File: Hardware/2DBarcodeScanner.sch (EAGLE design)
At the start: 25 parts, among them J1 BARCODE_ENGINE_CONN, Q1 600mA/40V, Q2 600mA/40V, U1 3.3V

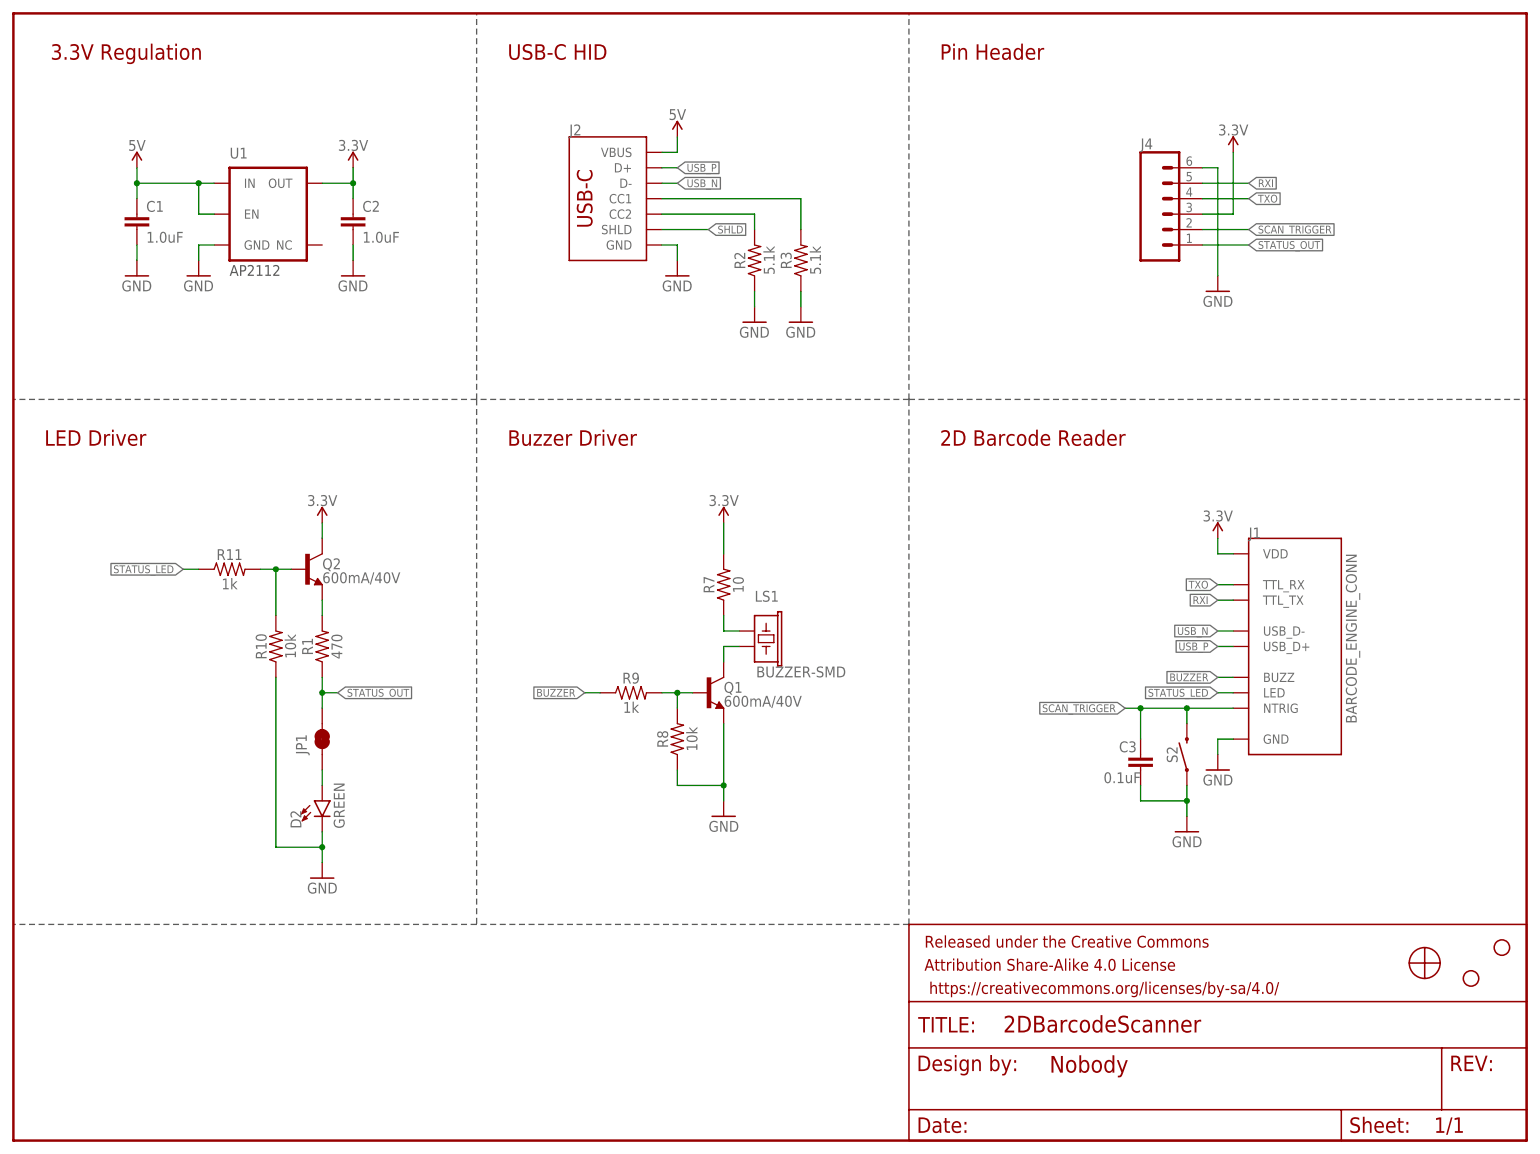
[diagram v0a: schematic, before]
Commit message: Update SPX design for reds
Changes made:
Switched out 12-pin ribbon cable connector for the one used on the RTK
Added jumper on the buzzer
Added power LED
Updated names/version numbers
Added fiducials
AND updated the barcode scanner footprint/silk
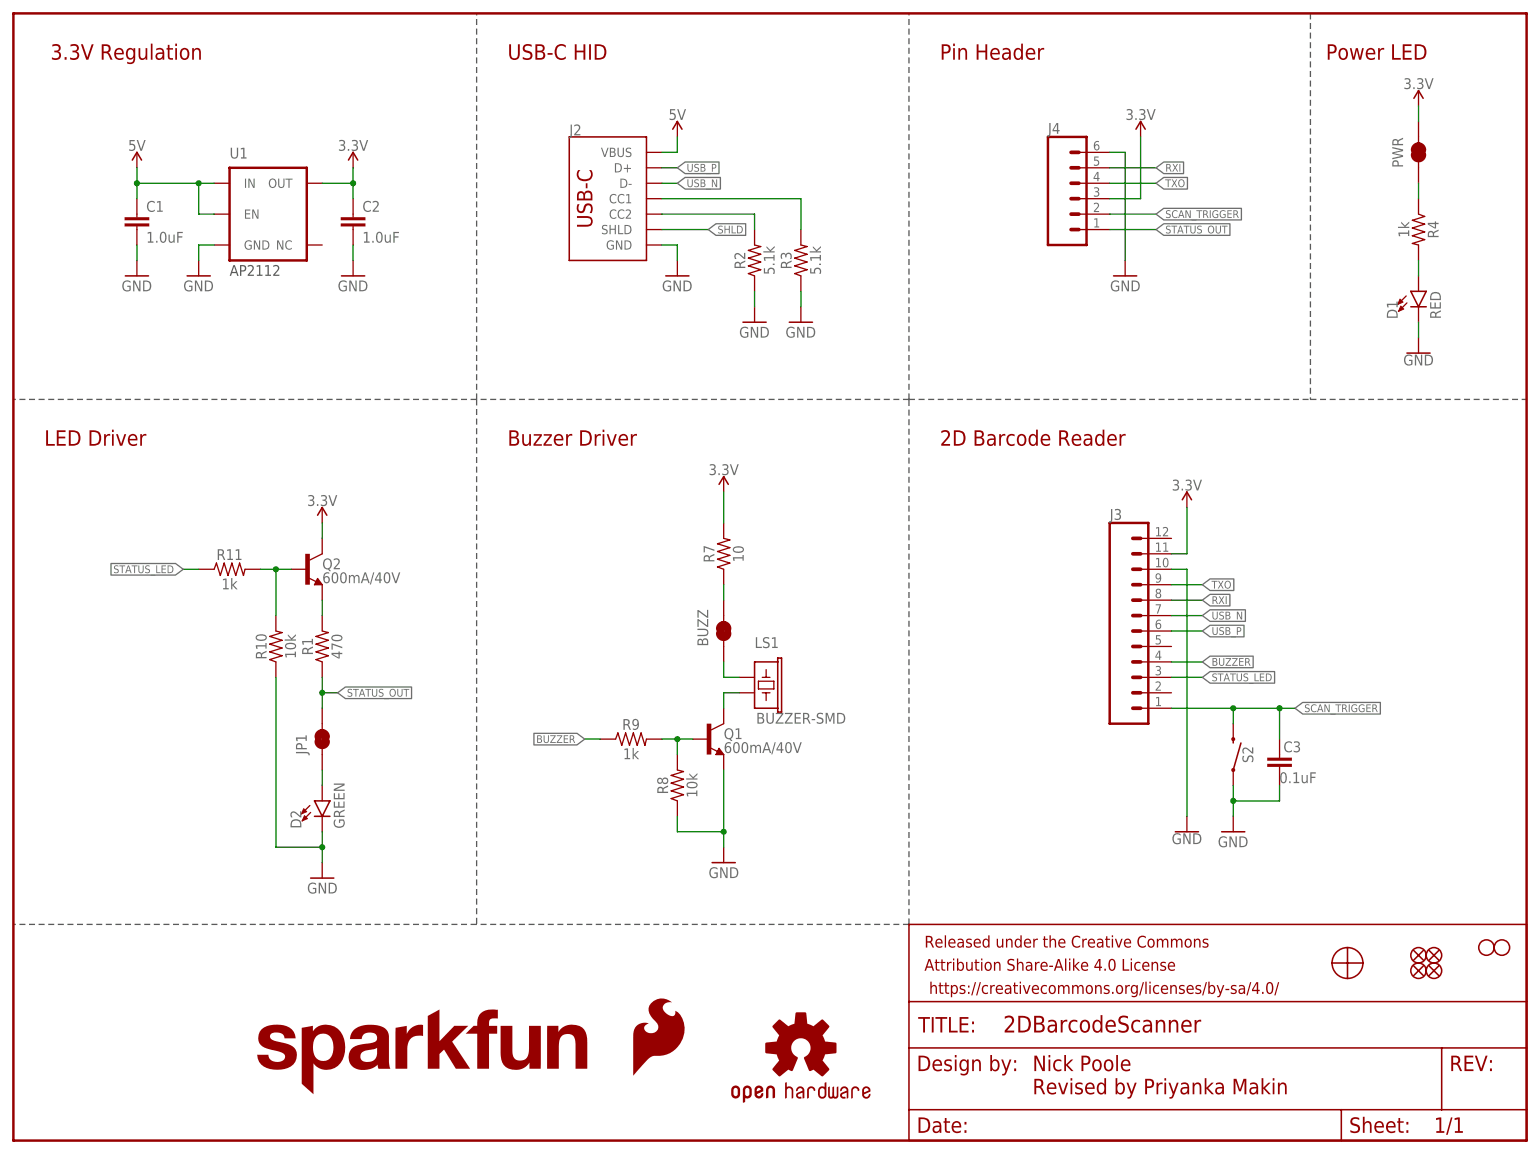
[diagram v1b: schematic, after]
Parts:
- removed J1: BARCODE_ENGINE_CONN, SparkFun-Connectors:BARCODE_ENGINE_CONN
- added BUZZ, PWR: JUMPER-SMT_2_NC_TRACE_SILK, SparkFun-Jumpers:JUMPER-SMT_2_NC_TRACE_SILK
- added D1: RED, SparkFun-LED:LED-RED0603
- added FD1, FD2, FD3, FD4: FIDUCIALUFIDUCIAL, SparkFun-Aesthetics:FIDUCIALUFIDUCIAL
- added J3: (no value), SparkFun-Connectors:CONN_12FPC_12_0.5MM
- added LOGO1: OSHW-LOGOS, SparkFun-Aesthetics:OSHW-LOGOS
- added LOGO2: SFE_LOGO_FLAME.2_INCH, SparkFun-Aesthetics:SFE_LOGO_FLAME.2_INCH
- added LOGO3: SFE_LOGO_NAME.1_INCH, SparkFun-Aesthetics:SFE_LOGO_NAME.1_INCH
- added R4: 1k, SparkFun-Resistors:1KOHM-0603-1/10W-1%
- J2: device SparkFun-Connectors:USB_C2-LAYER -> SparkFun-Connectors:USB_C_2-LAYER_PADS
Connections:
- new net N$1: BUZZ.2, R7.1
- new net N$6: PWR.1, R4.1
- new net N$9: D1.A, R4.2
- net 3.3V: now also J3.11, PWR.2; no longer J1.VDD
- net BUZZER: now also J3.4; no longer J1.BUZZ
- net GND: now also D1.C, J3.10; no longer J1.GND
- net N$3: now also BUZZ.1; no longer R7.1
- net RXI: now also J3.8; no longer J1.TTL_TX
- net SCAN_TRIGGER: now also J3.1; no longer J1.NTRIG
- net STATUS_LED: now also J3.3; no longer J1.LED
- net TXO: now also J3.9; no longer J1.TTL_RX
- net USB_N: now also J3.7; no longer J1.USB_D-
- net USB_P: now also J3.6; no longer J1.USB_D+
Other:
- note added: "Nick Poole Revised by Priyanka Makin"
- note added: "Power LED"
- moved on the sheet: C3, J4, LS1, Q1, R7, R8, R9, S2

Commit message: Update silkscreen
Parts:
- LOGO2: value SFE_LOGO_FLAME.2_INCH -> SFE_LOGO_FLAME.1_INCH; device SparkFun-Aesthetics:SFE_LOGO_FLAME.2_INCH -> SparkFun-Aesthetics:SFE_LOGO_FLAME.1_INCH
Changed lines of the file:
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@@
 <?xml version="1.0" encoding="utf-8"?>
 <!DOCTYPE eagle SYSTEM "eagle.dtd">
-<eagle version="9.5.2">
+<eagle version="9.6.2">
 <drawing>
 <settings>
@@
 <part name="BUZZ" library="SparkFun-Jumpers" deviceset="JUMPER-SMT_2_NC_TRACE" device="_SILK" package3d_urn="urn:adsk.eagle:package:39281/1"/>
 <part name="LOGO1" library="SparkFun-Aesthetics" deviceset="OSHW-LOGO" device="S"/>
-<part name="LOGO2" library="SparkFun-Aesthetics" deviceset="SFE_LOGO_FLAME" device=".2_INCH" value="SFE_LOGO_FLAME.2_INCH"/>
+<part name="LOGO2" library="SparkFun-Aesthetics" deviceset="SFE_LOGO_FLAME" device=".1_INCH" value="SFE_LOGO_FLAME.1_INCH"/>
 <part name="LOGO3" library="SparkFun-Aesthetics" deviceset="SFE_LOGO_NAME" device=".1_INCH"/>
 <part name="PWR" library="SparkFun-Jumpers" deviceset="JUMPER-SMT_2_NC_TRACE" device="_SILK" package3d_urn="urn:adsk.eagle:package:39281/1"/>

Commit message: Ran schematic/board checklists
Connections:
- removed net SHLD: J2.SHLD
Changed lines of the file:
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@@
 <?xml version="1.0" encoding="utf-8"?>
 <!DOCTYPE eagle SYSTEM "eagle.dtd">
-<eagle version="9.6.2">
+<eagle version="9.5.2">
 <drawing>
 <settings>
@@
 <grid distance="0.1" unitdist="inch" unit="inch" style="lines" multiple="1" display="no" altdistance="0.01" altunitdist="inch" altunit="inch"/>
 <layers>
-<layer number="1" name="Top" color="4" fill="1" visible="yes" active="no"/>
-<layer number="2" name="Route2" color="16" fill="1" visible="yes" active="no"/>
-<layer number="3" name="Route3" color="17" fill="1" visible="yes" active="no"/>
-<layer number="4" name="Route4" color="18" fill="1" visible="yes" active="no"/>
-<layer number="5" name="Route5" color="19" fill="1" visible="yes" active="no"/>
-<layer number="6" name="Route6" color="25" fill="1" visible="yes" active="no"/>
-<layer number="7" name="Route7" color="26" fill="1" visible="yes" active="no"/>
-<layer number="8" name="Route8" color="27" fill="1" visible="yes" active="no"/>
-<layer number="9" name="Route9" color="28" fill="1" visible="yes" active="no"/>
-<layer number="10" name="Route10" color="29" fill="1" visible="yes" active="no"/>
-<layer number="11" name="Route11" color="30" fill="1" visible="yes" active="no"/>
-<layer number="12" name="Route12" color="20" fill="1" visible="yes" active="no"/>
-<layer number="13" name="Route13" color="21" fill="1" visible="yes" active="no"/>
-<layer number="14" name="Route14" color="22" fill="1" visible="yes" active="no"/>
-<layer number="15" name="Route15" color="23" fill="1" visible="yes" active="no"/>
-<layer number="16" name="Bottom" color="1" fill="1" visible="yes" active="no"/>
-<layer number="17" name="Pads" color="2" fill="1" visible="yes" active="no"/>
-<layer number="18" name="Vias" color="2" fill="1" visible="yes" active="no"/>
-<layer number="19" name="Unrouted" color="6" fill="1" visible="yes" active="no"/>
-<layer number="20" name="Dimension" color="24" fill="1" visible="yes" active="no"/>
-<layer number="21" name="tPlace" color="16" fill="1" visible="yes" active="no"/>
-<layer number="22" name="bPlace" color="14" fill="1" visible="yes" active="no"/>
-<layer number="23" name="tOrigins" color="15" fill="1" visible="yes" active="no"/>
-<layer number="24" name="bOrigins" color="15" fill="1" visible="yes" active="no"/>
-<layer number="25" name="tNames" color="7" fill="1" visible="yes" active="no"/>
-<layer number="26" name="bNames" color="7" fill="1" visible="yes" active="no"/>
-<layer number="27" name="tValues" color="7" fill="1" visible="yes" active="no"/>
-<layer number="28" name="bValues" color="7" fill="1" visible="yes" active="no"/>
+<layer number="1" name="Top" color="4" fill="1" visible="no" active="no"/>
+<layer number="2" name="Route2" color="16" fill="1" visible="no" active="no"/>
+<layer number="3" name="Route3" color="17" fill="1" visible="no" active="no"/>
+<layer number="4" name="Route4" color="18" fill="1" visible="no" active="no"/>
+<layer number="5" name="Route5" color="19" fill="1" visible="no" active="no"/>
+<layer number="6" name="Route6" color="25" fill="1" visible="no" active="no"/>
+<layer number="7" name="Route7" color="26" fill="1" visible="no" active="no"/>
+<layer number="8" name="Route8" color="27" fill="1" visible="no" active="no"/>
+<layer number="9" name="Route9" color="28" fill="1" visible="no" active="no"/>
+<layer number="10" name="Route10" color="29" fill="1" visible="no" active="no"/>
+<layer number="11" name="Route11" color="30" fill="1" visible="no" active="no"/>
+<layer number="12" name="Route12" color="20" fill="1" visible="no" active="no"/>
+<layer number="13" name="Route13" color="21" fill="1" visible="no" active="no"/>
+<layer number="14" name="Route14" color="22" fill="1" visible="no" active="no"/>
+<layer number="15" name="Route15" color="23" fill="1" visible="no" active="no"/>
+<layer number="16" name="Bottom" color="1" fill="1" visible="no" active="no"/>
+<layer number="17" name="Pads" color="2" fill="1" visible="no" active="no"/>
+<layer number="18" name="Vias" color="2" fill="1" visible="no" active="no"/>
+<layer number="19" name="Unrouted" color="6" fill="1" visible="no" active="no"/>
+<layer number="20" name="Dimension" color="24" fill="1" visible="no" active="no"/>
+<layer number="21" name="tPlace" color="16" fill="1" visible="no" active="no"/>
+<layer number="22" name="bPlace" color="14" fill="1" visible="no" active="no"/>
+<layer number="23" name="tOrigins" color="15" fill="1" visible="no" active="no"/>
+<layer number="24" name="bOrigins" color="15" fill="1" visible="no" active="no"/>
+<layer number="25" name="tNames" color="7" fill="1" visible="no" active="no"/>
+<layer number="26" name="bNames" color="7" fill="1" visible="no" active="no"/>
+<layer number="27" name="tValues" color="7" fill="1" visible="no" active="no"/>
+<layer number="28" name="bValues" color="7" fill="1" visible="no" active="no"/>
 <layer number="29" name="tStop" color="7" fill="3" visible="no" active="no"/>
 <layer number="30" name="bStop" color="7" fill="6" visible="no" active="no"/>
@@
 <layer number="35" name="tGlue" color="7" fill="4" visible="no" active="no"/>
 <layer number="36" name="bGlue" color="7" fill="5" visible="no" active="no"/>
-<layer number="37" name="tTest" color="7" fill="1" visible="yes" active="no"/>
-<layer number="38" name="bTest" color="7" fill="1" visible="yes" active="no"/>
+<layer number="37" name="tTest" color="7" fill="1" visible="no" active="no"/>
+<layer number="38" name="bTest" color="7" fill="1" visible="no" active="no"/>
 <layer number="39" name="tKeepout" color="4" fill="11" visible="no" active="no"/>
 <layer number="40" name="bKeepout" color="1" fill="11" visible="no" active="no"/>
@@
 <layer number="44" name="Drills" color="7" fill="1" visible="no" active="no"/>
 <layer number="45" name="Holes" color="7" fill="1" visible="no" active="no"/>
-<layer number="46" name="Milling" color="3" fill="1" visible="yes" active="no"/>
-<layer number="47" name="Measures" color="7" fill="1" visible="yes" active="no"/>
-<layer number="48" name="Document" color="7" fill="1" visible="yes" active="no"/>
-<layer number="49" name="Reference" color="7" fill="1" visible="yes" active="no"/>
-<layer number="50" name="dxf" color="7" fill="1" visible="yes" active="no"/>
-<layer number="51" name="tDocu" color="6" fill="1" visible="yes" active="no"/>
-<layer number="52" name="bDocu" color="7" fill="1" visible="yes" active="no"/>
-<layer number="53" name="tGND_GNDA" color="7" fill="9" visible="yes" active="no"/>
-<layer number="54" name="bGND_GNDA" color="1" fill="9" visible="yes" active="no"/>
-<layer number="56" name="wert" color="7" fill="1" visible="yes" active="no"/>
-<layer number="57" name="tCAD" color="7" fill="1" visible="yes" active="no"/>
-<layer number="59" name="tCarbon" color="7" fill="1" visible="yes" active="no"/>
-<layer number="60" name="bCarbon" color="7" fill="1" visible="yes" active="no"/>
+<layer number="46" name="Milling" color="3" fill="1" visible="no" active="no"/>
+<layer number="47" name="Measures" color="7" fill="1" visible="no" active="no"/>
+<layer number="48" name="Document" color="7" fill="1" visible="no" active="no"/>
+<layer number="49" name="Reference" color="7" fill="1" visible="no" active="no"/>
+<layer number="50" name="dxf" color="7" fill="1" visible="no" active="no"/>
+<layer number="51" name="tDocu" color="6" fill="1" visible="no" active="no"/>
+<layer number="52" name="bDocu" color="7" fill="1" visible="no" active="no"/>
+<layer number="53" name="tGND_GNDA" color="7" fill="9" visible="no" active="no"/>
+<layer number="54" name="bGND_GNDA" color="1" fill="9" visible="no" active="no"/>
+<layer number="56" name="wert" color="7" fill="1" visible="no" active="no"/>
+<layer number="57" name="tCAD" color="7" fill="1" visible="no" active="no"/>
+<layer number="59" name="tCarbon" color="7" fill="1" visible="no" active="no"/>
+<layer number="60" name="bCarbon" color="7" fill="1" visible="no" active="no"/>
 <layer number="88" name="SimResults" color="9" fill="1" visible="yes" active="yes"/>
 <layer number="89" name="SimProbes" color="9" fill="1" visible="yes" active="yes"/>
@@
 <plain>
 <text x="6.096" y="177.8" size="2.54" layer="94" font="vector">3.3V Regulation</text>
-<text x="35.56" y="142.24" size="1.778" layer="97">AP2112</text>
+<text x="35.56" y="142.24" size="1.778" layer="97" font="vector">AP2112</text>
 <wire x1="147.32" y1="35.56" x2="76.2" y2="35.56" width="0.2032" layer="97" style="longdash"/>
 <text x="152.4" y="177.8" size="2.54" layer="94" font="vector">Pin Header</text>
@@
 </segment>
 </net>
-<net name="SHLD" class="0">
-<segment>
-<pinref part="J2" gate="J1" pin="SHLD"/>
-<wire x1="106.68" y1="149.86" x2="114.3" y2="149.86" width="0.1524" layer="91"/>
-<label x="114.3" y="149.86" size="1.27" layer="95" xref="yes"/>
-</segment>
-</net>
